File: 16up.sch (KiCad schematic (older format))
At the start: 29 parts, among them CN1 EXPANSION_PORT, CN2 ALMOST_USERPORT, CN3 DB9_MALE, CN4 TAPE_IN, J1 ATTENTION_IN, U1 GAL20V8, U102 74LS652, U2 MOS_6529, U3 MOS_6551_ACIA, U4 MAX238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

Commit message: Start 232-less version
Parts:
- removed C4, C5, C6, C7, C8: 1u, Capacitor_THT:CP_Radial_D5.0mm_P2.00mm, symbol Device:CP1
- removed CN3: DB9_MALE, 16up:DB_9M, symbol Connector:DB9_Male_MountingHoles
- removed D1: BAT43, Diode_THT:D_DO-35_SOD27_P2.54mm_Vertical_KathodeUp, symbol Device:D
- removed JP2: JMP_CTS_IN, Connector_PinHeader_2.54mm:PinHeader_1x03_P2.54mm_Vertical, symbol Connector:Conn_01x03_Male
- removed JP3: JMP_CTS_ACIA, Connector_PinHeader_2.54mm:PinHeader_1x03_P2.54mm_Vertical, symbol Connector:Conn_01x03_Male
- removed R3: 10k, Resistor_THT:R_Axial_DIN0207_L6.3mm_D2.5mm_P2.54mm_Vertical, symbol Device:R
- removed U4: MAX238, Package_DIP:DIP-24_W7.62mm_Socket_LongPads, symbol MAX238:MAX238
- added C4: 100n, Capacitor_THT:C_Disc_D7.0mm_W2.5mm_P5.00mm, symbol Device:C
- added U4: 74HCT04, Package_DIP:DIP-14_W7.62mm_Socket_LongPads, symbol 74xx:74HCT04
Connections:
- net ~dcd is gone; now on net +5V: R1.2
- net ~dsr is gone; now on net dcd_ttl: R2.2
- net +5V: now also R2.1, C4.1, U4.14 (VCC)
- net GND: now also U3.9 (~CTS), C4.2, U4.7 (GND)
- net rxd_ttl: now also CN2.C (RXD)
- net txd_ttl: now also CN2.M (TXD)
- net ~dcd_ttl: now also U4.2
- net ~dsr_ttl: now also U4.12
- net ~dtr_ttl: now also U4.3
- net ~rts_ttl: now also U4.5
- net rxc: now reaches CN2.8 (RXC)
- net rxc: now also U3.5 (RXC)
- net rts_ttl: now reaches CN2.D (RTS)
- net rts_ttl: now also U4.6
- net dtr_ttl: now reaches CN2.E (DTR)
- net dtr_ttl: now also U4.4
- net dcd_ttl: now reaches CN2.H (DCD)
- net dcd_ttl: now also U4.1
- net dsr_ttl: now reaches CN2.L (DSR)
- net dsr_ttl: now also R1.1, U4.13
- removed net +12V: R1.1, R2.1
- net cts_ttl: no longer names the net of U1.17 (IO17)
- net ~cts_ttl: no longer names the net of U1.18 (IO18)
- no-connect marks 35 -> 29
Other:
- note added: "SPARES"
- note removed: "MMMH... MAYBE RI COULD\nBE CONNECTED TO A\nDATA PIN SOMEHOW?"
- note removed: "RS-232 PORT"
- note removed: "THE KERNAL EXPECTS THE ~CTS~ SIGNAL\nTO BE ACTIVE-HIGH, SO WE INVERT IT\nTHROUGH THE GAL. THE DIODE EMULATES\nAN OPEN-COLLECTOR OUTPUT.\n\nNOTE THAT FOR THIS TO WORK, THE 6529\nOUTPUTS MUST BE HIGH WHEN USING THE\nSERIAL PORT, WHICH IS THE CASE AT\nPOWER-UP/RESET."
- note removed: "TTL-RS-232 LEVEL SHIFTING"

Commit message: Routing done
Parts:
- removed J1: ATTENTION_IN, Connector_PinHeader_2.54mm:PinHeader_1x01_P2.54mm_Vertical, symbol Connector:Conn_01x01_Male
- added J3: CONN_UPORT254, Connector_PinHeader_2.54mm:PinHeader_2x12_P2.54mm_Vertical, symbol Connector_Generic:Conn_02x12_Odd_Even
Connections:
- net +5V: now also J3.4 (Pin_4)
- net GND: now also J3.1 (Pin_1), J3.2 (Pin_2), J3.23 (Pin_23), J3.24 (Pin_24)
- net dcd_ttl: now also J3.13 (Pin_13)
- net dsr_ttl: now also J3.19 (Pin_19)
- net dtr_ttl: now also J3.9 (Pin_9)
- net p0: now also J3.3 (Pin_3)
- net p1: now also J3.17 (Pin_17)
- net p2: now also J3.8 (Pin_8)
- net p3: now also J3.10 (Pin_10)
- net p4: now also J3.12 (Pin_12)
- net p5: now also J3.14 (Pin_14)
- net p6: now also J3.15 (Pin_15)
- net p7: now also J3.11 (Pin_11)
- net rts_ttl: now also J3.7 (Pin_7)
- net rxc: now also J3.16 (Pin_16)
- net rxd_ttl: now also J3.5 (Pin_5)
- net txd_ttl: now also J3.21 (Pin_21)
- net ~reset: now also J3.6 (Pin_6)
- net +9v: now reaches CN2.10 (+9VAC)
- net +9v: now also J3.20 (Pin_20)
- net -9v: now reaches CN2.11 (-9VAC)
- net -9v: now also J3.22 (Pin_22)
- net ~attn: now reaches CN2.9 (~ATTN)
- net ~attn: now also J3.18 (Pin_18)
- no-connect marks 29 -> 27
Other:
- note added: "IMPORTANT:\n~ATTN~ and +/-9V MUST BE\nPROVIDED EXTERNALLY\nTHROUGH J3, IF NEEDED!"
- note added: "THESE COMPONENTS ARE NEEDED TO MAKE THE 74x654 OUTPUTS\nBEHAVE IN AN OPEN-COLLECTOR FASHION, AS THE ORIGINAL MOS\n6529 OUTPUTS DO.\n\nTHEY MUST BE PLACED THIS WAY (I.E. AFTER THE OUTPUTS EVEN IF\nAN ORIGINAL 6529 IS USED) FOR ROUTING REASONS, THEREFORE IF\n74x654 OR ORIGINAL MOS 6529 IS USED, REPLACE D1-8 WITH\n0-OHM RESISTORS.\n\nIF ORIGINAL MOS 6529 IS USED, DO NOT MOUNT RN1 EITHER."
- note added: "USER PORT PIN HEADER"
- note removed: "NO WAY WE\nCAN HAVE\n9VAC HERE!"
- note removed: "SINCE WE HAVE A MAX238 ONBOARD,\nSERIAL SIGNALS ARE NOT CONNECTED"
- note removed: "THESE COMPONENTS ARE NEEDED TO MAKE THE 74x652 OUTPUTS\nBEHAVE IN AN OPEN-COLLECTOR FASHION, AS THE ORIGINAL MOS\n6529 OUTPUTS DO.\n\nTHEY MUST BE PLACED THIS WAY (I.E. AFTER THE OUTPUTS EVEN IF\nAN ORIGINAL 6529 IS USED) FOR ROUTING REASONS, THEREFORE IF\n74x654 OR ORIGINAL MOS 6529 IS USED, REPLACE D1-8 WITH\n0-OHM RESISTORS.\n\nIF ORIGINAL MOS 6529 IS USED, DO NOT MOUNT RN1 EITHER."
- note removed: "WE PROVIDE A PIN\nFOR CONNECTION\nTO REAL ~ATTN~ LINE,\nJUST IN CASE"
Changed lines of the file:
@@
 Sheet 1 1
 Title "16up"
-Date "2023-03-07"
+Date "2023-03-13"
 Rev "3git"
 Comp "SukkoPera & The Folks From The Plus/4 World Forum"
@@
 Text Label 15780 1760 2    50   ~ 0
 p7
-NoConn ~ 13805 2160
-NoConn ~ 13805 2260
 Wire Wire Line
 	13805 1460 13430 1460
@@
 	13155 2990 15880 2990
 Connection ~ 13155 2990
-$Comp
-L Connector:Conn_01x01_Male J1
-U 1 1 65389334
-P 12635 2060
-F 0 "J1" H 12745 2285 50  0000 C CNN
-F 1 "ATTENTION_IN" H 12745 2190 50  0000 C CNN
-F 2 "Connector_PinHeader_2.54mm:PinHeader_1x01_P2.54mm_Vertical" H 12635 2060 50  0001 C CNN
-F 3 "~" H 12635 2060 50  0001 C CNN
-	1    12635 2060
-	1    0    0    -1
-$EndComp
-Wire Wire Line
-	12835 2060 13805 2060
-Text Notes 12980 2465 2    50   ~ 0
-WE PROVIDE A PIN\nFOR CONNECTION\nTO REAL ~ATTN~ LINE,\nJUST IN CASE
+Text Notes 14985 3415 2    50   ~ 0
+IMPORTANT:\n~ATTN~ and +/-9V MUST BE\nPROVIDED EXTERNALLY\nTHROUGH J3, IF NEEDED!
 Text Notes 10385 1050 0    50   ~ 0
 "PARALLEL" PORT
 Text Notes 14105 745  0    50   ~ 0
 USER PORT CONNECTOR
-Text Notes 13675 2355 2    50   ~ 0
-NO WAY WE\nCAN HAVE\n9VAC HERE!
 Wire Wire Line
 	9955 1895 9680 1895
@@
 Wire Wire Line
 	1240 4005 1580 4005
-Text Notes 13845 3245 0    50   ~ 0
-SINCE WE HAVE A MAX238 ONBOARD,\nSERIAL SIGNALS ARE NOT CONNECTED
 Text Notes 2795 7005 2    50   ~ 0
 NOTE THAT THE +4 USER PORT HAS NO DEDICATED\n~CTS~ PIN. THIS COULD BE BECAUSE OF A BUG IN\nTHE 6551 THAT CAUSED TRANSMISSIONS TO BE ABORTED\n*IMMEDIATELY* WHEN ~CTS~ WAS DEASSERTED, RATHER\nTHAN AFTER THE BYTE CURRENTLY BEING TRANSMITTED.\nTHE SIGNAL IS EXPECTED ON PIN K ON THE USER PORT\nCONNECTOR INSTEAD (EXACTLY WHERE IT WOULD BE ON\nTHE C64), WHICH IS CONNECTED TO D1, AND HANDLED\nBY THE KERNAL.
@@
 Text Notes 8430 3735 0    50   ~ 0
 MOS 6529 REPLACEMENT CIRCUIT\nBY DANIEL MANTIONE
-Text Notes 10400 6330 0    50   ~ 0
-THESE COMPONENTS ARE NEEDED TO MAKE THE 74x652 OUTPUTS\nBEHAVE IN AN OPEN-COLLECTOR FASHION, AS THE ORIGINAL MOS\n6529 OUTPUTS DO.\n\nTHEY MUST BE PLACED THIS WAY (I.E. AFTER THE OUTPUTS EVEN IF\nAN ORIGINAL 6529 IS USED) FOR ROUTING REASONS, THEREFORE IF\n74x654 OR ORIGINAL MOS 6529 IS USED, REPLACE D1-8 WITH\n0-OHM RESISTORS.\n\nIF ORIGINAL MOS 6529 IS USED, DO NOT MOUNT RN1 EITHER.
+Text Notes 9365 6320 0    50   ~ 0
+THESE COMPONENTS ARE NEEDED TO MAKE THE 74x654 OUTPUTS\nBEHAVE IN AN OPEN-COLLECTOR FASHION, AS THE ORIGINAL MOS\n6529 OUTPUTS DO.\n\nTHEY MUST BE PLACED THIS WAY (I.E. AFTER THE OUTPUTS EVEN IF\nAN ORIGINAL 6529 IS USED) FOR ROUTING REASONS, THEREFORE IF\n74x654 OR ORIGINAL MOS 6529 IS USED, REPLACE D1-8 WITH\n0-OHM RESISTORS.\n\nIF ORIGINAL MOS 6529 IS USED, DO NOT MOUNT RN1 EITHER.
 Text Label 11730 2595 2    50   ~ 0
 p7
@@
 	1    0    0    -1
 $EndComp
+Wire Wire Line
+	14190 5170 14100 5170
+Wire Wire Line
+	14100 5170 14100 6270
+Wire Wire Line
+	14190 6270 14100 6270
+Connection ~ 14100 6270
+Wire Wire Line
+	14100 6270 14100 6535
+$Comp
+L power:GND #PWR05
+U 1 1 6418AC8A
+P 14100 6535
+F 0 "#PWR05" H 14100 6285 50  0001 C CNN
+F 1 "GND" H 14105 6362 50  0000 C CNN
+F 2 "" H 14100 6535 50  0001 C CNN
+F 3 "" H 14100 6535 50  0001 C CNN
+	1    14100 6535
+	1    0    0    -1
+$EndComp
+Wire Wire Line
+	14690 5170 14795 5170
+Wire Wire Line
+	14795 5170 14795 6270
+Wire Wire Line
+	14690 6270 14795 6270
+Connection ~ 14795 6270
+Wire Wire Line
+	14795 6270 14795 6535
+$Comp
+L power:GND #PWR06
+U 1 1 6418AC99
+P 14795 6535
+F 0 "#PWR06" H 14795 6285 50  0001 C CNN
+F 1 "GND" H 14800 6362 50  0000 C CNN
+F 2 "" H 14795 6535 50  0001 C CNN
+F 3 "" H 14795 6535 50  0001 C CNN
+	1    14795 6535
+	-1   0    0    -1
+$EndComp
+Wire Wire Line
+	13925 5270 13925 4805
+$Comp
+L power:+5V #PWR03
+U 1 1 6418ACA5
+P 13925 4805
+F 0 "#PWR03" H 13925 4655 50  0001 C CNN
+F 1 "+5V" H 13940 4978 50  0000 C CNN
+F 2 "" H 13925 4805 50  0001 C CNN
+F 3 "" H 13925 4805 50  0001 C CNN
+	1    13925 4805
+	1    0    0    -1
+$EndComp
+Wire Wire Line
+	14690 5270 15165 5270
+Wire Wire Line
+	14690 5970 15165 5970
+Wire Wire Line
+	14690 5870 15165 5870
+Wire Wire Line
+	14690 5670 15165 5670
+Entry Wire Line
+	13540 5570 13640 5470
+Entry Wire Line
+	13540 5670 13640 5570
+Entry Wire Line
+	13540 5770 13640 5670
+Entry Wire Line
+	13540 5870 13640 5770
+Entry Wire Line
+	15265 5370 15165 5270
+Entry Wire Line
+	15265 6070 15165 5970
+Entry Wire Line
+	15265 5970 15165 5870
+Entry Wire Line
+	15265 5770 15165 5670
+Wire Bus Line
+	13540 6900 12890 6900
+Text Label 12890 6900 0    50   ~ 0
+parallel_port
+Text Label 13640 5470 0    50   ~ 0
+p2
+Text Label 13640 5570 0    50   ~ 0
+p3
+Text Label 13640 5670 0    50   ~ 0
+p4
+Text Label 13640 5770 0    50   ~ 0
+p5
+Text Label 15165 5270 2    50   ~ 0
+p0
+Text Label 15165 5970 2    50   ~ 0
+p1
+Text Label 15165 5870 2    50   ~ 0
+p6
+Text Label 15165 5670 2    50   ~ 0
+p7
+Text Label 13815 5370 0    50   ~ 0
+~reset
+Wire Bus Line
+	13540 6900 15265 6900
+Connection ~ 13540 6900
+Text Notes 14005 4475 0    50   ~ 0
+USER PORT PIN HEADER
+Text Label 13815 5870 0    50   ~ 0
+rxc
+Wire Wire Line
+	14690 5370 15065 5370
+Text Label 15065 5370 2    50   ~ 0
+rxd_ttl
+Wire Wire Line
+	14690 5470 15065 5470
+Wire Wire Line
+	14690 5570 15065 5570
+Wire Wire Line
+	14690 5770 15065 5770
+Text Label 15065 5470 2    50   ~ 0
+rts_ttl
+Text Label 15065 5570 2    50   ~ 0
+dtr_ttl
+Text Label 15065 5770 2    50   ~ 0
+dcd_ttl
+Wire Wire Line
+	14690 6070 15065 6070
+Wire Wire Line
+	14690 6170 15065 6170
+Text Label 15065 6070 2    50   ~ 0
+dsr_ttl
+Text Label 15065 6170 2    50   ~ 0
+txd_ttl
+Text Label 13430 2060 0    50   ~ 0
+~attn
+Text Label 13815 5970 0    50   ~ 0
+~attn
+Wire Wire Line
+	14190 5470 13640 5470
+Wire Wire Line
+	14190 5370 13815 5370
+Wire Wire Line
+	14190 5270 13925 5270
+Wire Wire Line
+	14190 5970 13815 5970
+Wire Wire Line
+	14190 5870 13815 5870
+Wire Wire Line
+	14190 5770 13640 5770
+Wire Wire Line
+	14190 5670 13640 5670
+Wire Wire Line
+	14190 5570 13640 5570
+$Comp
+L Connector_Generic:Conn_02x12_Odd_Even J3
+U 1 1 641A7782
+P 14490 5670
+F 0 "J3" H 14540 6387 50  0000 C CNN
+F 1 "CONN_UPORT254" H 14540 6296 50  0000 C CNN
+F 2 "Connector_PinHeader_2.54mm:PinHeader_2x12_P2.54mm_Vertical" H 14490 5670 50  0001 C CNN
+F 3 "~" H 14490 5670 50  0001 C CNN
+	1    14490 5670
+	-1   0    0    -1
+$EndComp
+Wire Wire Line
+	13805 2160 13430 2160
+Wire Wire Line
+	13805 2260 13430 2260
+Text Label 13430 2160 0    50   ~ 0
++9v
+Text Label 13430 2260 0    50   ~ 0
+-9v
+Wire Wire Line
+	14190 6070 13815 6070
+Wire Wire Line
+	14190 6170 13815 6170
+Text Label 13815 6070 0    50   ~ 0
++9v
+Text Label 13815 6170 0    50   ~ 0
+-9v
+Wire Wire Line
+	13805 2060 13430 2060
+Wire Bus Line
+	15265 5370 15265 6900
+Wire Bus Line
+	13540 5570 13540 6900
 Wire Bus Line
 	15880 1460 15880 2990

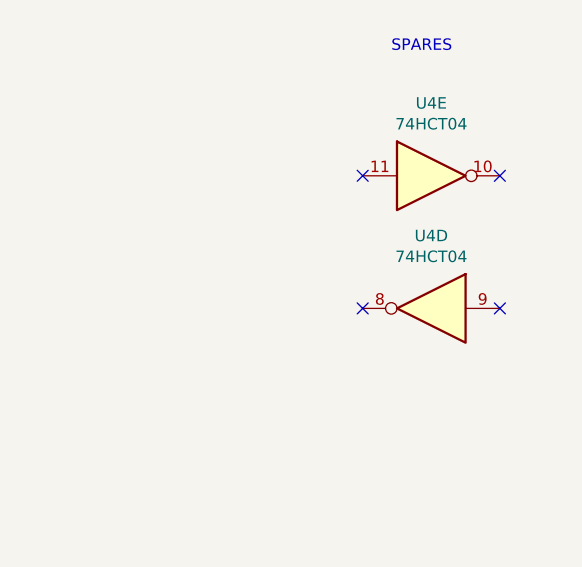
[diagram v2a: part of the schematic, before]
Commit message: Ground unused gates of U4
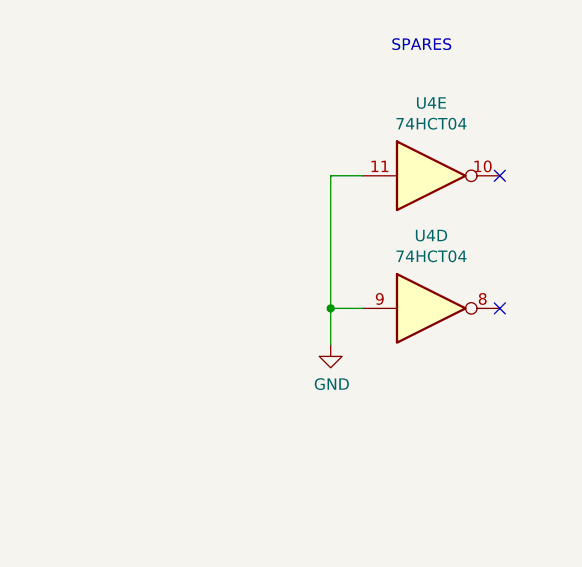
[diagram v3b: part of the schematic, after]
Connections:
- net GND: now also U4.11, U4.9
- no-connect marks 27 -> 25
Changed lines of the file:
@@
 F 3 "https://assets.nexperia.com/documents/data-sheet/74HC_HCT04.pdf" H 15300 9465 50  0001 C CNN
 	4    15300 9465
-	-1   0    0    -1
+	1    0    0    -1
 $EndComp
 $Comp
@@
 	1    0    0    -1
 $EndComp
-NoConn ~ 15000 8885
-NoConn ~ 15000 9465
-NoConn ~ 15600 9465
 NoConn ~ 15600 8885
 Text Notes 15125 8350 0    50   ~ 0
@@
 Wire Wire Line
 	13805 2060 13430 2060
+NoConn ~ 15600 9465
+Wire Wire Line
+	15000 8885 14860 8885
+Wire Wire Line
+	14860 8885 14860 9465
+Wire Wire Line
+	15000 9465 14860 9465
 Wire Bus Line
 	15265 5370 15265 6900
@@
 Wire Bus Line
 	5500 1470 5500 2575
+Connection ~ 14860 9465
+Wire Wire Line
+	14860 9465 14860 9625
+$Comp
+L power:GND #PWR?
+U 1 1 6455627D
+P 14860 9625
+F 0 "#PWR?" H 14860 9375 50  0001 C CNN
+F 1 "GND" H 14865 9452 50  0000 C CNN
+F 2 "" H 14860 9625 50  0001 C CNN
+F 3 "" H 14860 9625 50  0001 C CNN
+	1    14860 9625
+	1    0    0    -1
+$EndComp
 $EndSCHEMATC

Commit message: Close #3
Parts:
- C2, C4: MouserPN (none) -> 810-FG28X7R1H104KNT0
- CN1, CN2, V0, V1: MouserPN (none) -> ---
- RN1: Notes (none) -> Do not mount if original MOS 6529 is used at U2
- U1: MouserPN (none) -> 556-AF22V10C15PU; Notes (none) -> Either GAL20V8 or GAL22V10 will work
- U102: value 74LS652 -> 74LS654; Notes (none) -> Either mount this OR U2
- U2: Notes (none) -> Either mount this OR U102
- Y1: MouserPN (none) -> 520-HCA184-SX; Notes (none) -> Use SERIES crystal
- renumbered J3 to CN3
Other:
- note added: "DO NOT MOUNT IF ORIGINAL\nMOS 6529 IS USED AT U2"
- note added: "MOS 6529 REPLACEMENT CIRCUIT\nBY DANIEL MANTIONE\n(ALTERNATIVE TO U2)"
- note added: "OR GAL22V10"
- note removed: "MOS 6529 REPLACEMENT CIRCUIT\nBY DANIEL MANTIONE"
- note removed: "OR GAL22V16"
- note removed: "THESE COMPONENTS ARE NEEDED TO MAKE THE 74x654 OUTPUTS\nBEHAVE IN AN OPEN-COLLECTOR FASHION, AS THE ORIGINAL MOS\n6529 OUTPUTS DO.\n\nTHEY MUST BE PLACED THIS WAY (I.E. AFTER THE OUTPUTS EVEN IF\nAN ORIGINAL 6529 IS USED) FOR ROUTING REASONS, THEREFORE IF\n74x654 OR ORIGINAL MOS 6529 IS USED, REPLACE D1-8 WITH\n0-OHM RESISTORS.\n\nIF ORIGINAL MOS 6529 IS USED, DO NOT MOUNT RN1 EITHER."
- moved on the sheet: RN1, U102
